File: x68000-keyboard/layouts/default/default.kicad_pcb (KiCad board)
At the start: 4 copper layers, 29.6 x 12.2 mm, 15 parts

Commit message: 両基板: MCU〜レベルシフタ間の信号ネットに用途名を付与
物理ピン名 (PB8, PA3 など) のままでは .ato ソースも生成回路図/ネットリスト
も読みづらいため、MCU 側〜レベルシフタ A 側に中間 signal を挿し、
has_net_name トレイトで用途名 (KEY_TXD_3V3, UP_3V3 など) を割り当てる。
KiCad 上のネット名表示も意味のある名前になる。

Co-Authored-By: Claude Opus 4.7 (1M context) <noreply@anthropic.com>
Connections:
- net PB10 renamed KEY_RXD_3V3
- net PB11 renamed KEY_TXD_3V3
- net PB12_T1C4_T2C2N_ renamed READY_3V3
- net PB8 renamed REMOTE_3V3
- net PB9_T1C1_MCO_TX4_ renamed MSDATA_3V3
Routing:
- net GND: track 4.00 -> 7.88 mm, vias 2 -> 3

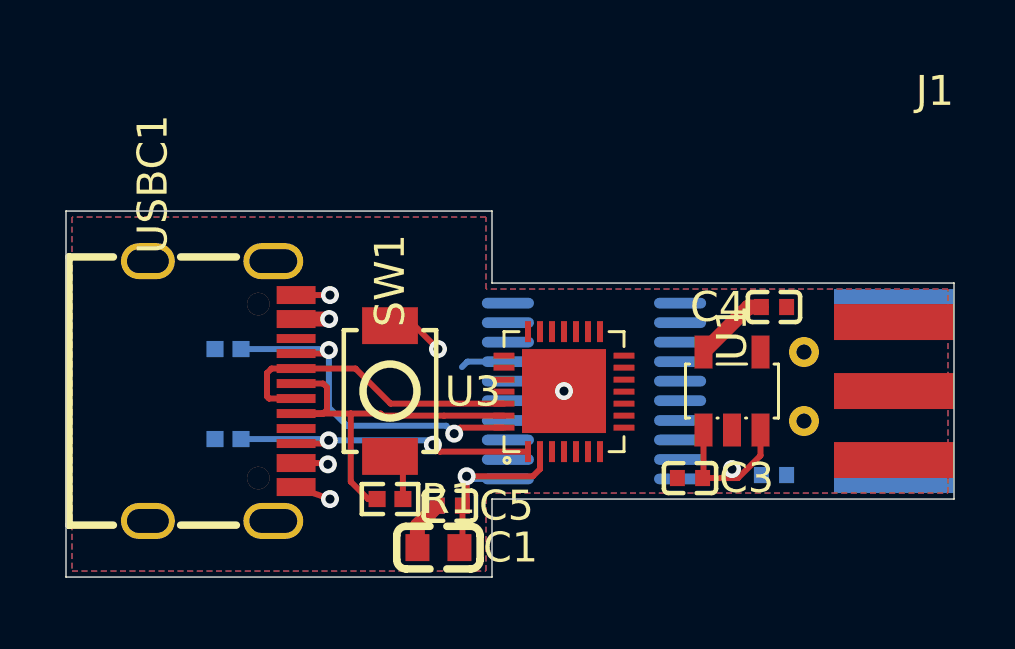
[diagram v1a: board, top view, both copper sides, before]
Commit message: x68000-keyboard: PCB レイアウト初版完了
PCB の配置と配線を一通り完了。レイアウトを進めるうえでフットプリントと
レベルシフタ割当も以下のように調整した。

- レベルシフタのチャネル割当を a1〜a5 から a4〜a8 に変更 (配線取り回しを
  優先)。未使用となった a1〜a3 は GND 落としに切り替え。
- Mini-DIN 7pin: ピン 1/2 のスルーホールパッドを 1.0mm → 0.8mm に縮小、
  ドリルは 0.5mm 維持
- USB-C コネクタフットプリント: pcbnew 上でシルク / 機械パッド表記を整理

DRC 警告は一部残置 (次のパスで詰める)。

Co-Authored-By: Claude Opus 4.7 (1M context) <noreply@anthropic.com>
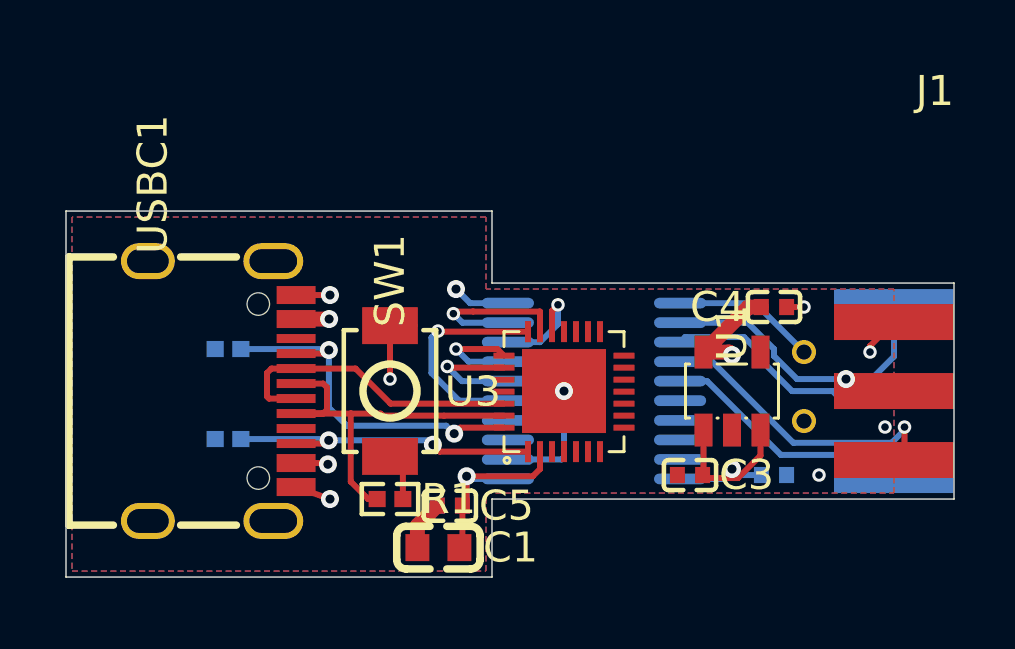
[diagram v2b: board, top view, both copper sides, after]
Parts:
- moved C3 0.10 mm to (171.2, 98.8)
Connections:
- U2 pad 11: b8 -> msdata
- U2 pad 12: b7 -> remote
- U2 pad 13: b6 -> key_txd
- U2 pad 14: remote -> ready
- U2 pad 15: msdata -> key_rxd
- U2 pad 16: ready -> b3
- U2 pad 17: key_rxd -> b2
- U2 pad 18: key_txd -> b1
- U2 pad 2: KEY_TXD_3V3 -> GND
- U2 pad 3: KEY_RXD_3V3 -> GND
- U2 pad 4: READY_3V3 -> GND
- U2 pad 5: MSDATA_3V3 -> KEY_RXD_3V3
- U2 pad 6: REMOTE_3V3 -> READY_3V3
- U2 pad 7: GND -> KEY_TXD_3V3
- U2 pad 8: GND -> REMOTE_3V3
- U2 pad 9: GND -> MSDATA_3V3
- USBC1 pad 1: shell -> GND
- USBC1 pad 2: shell -> GND
- USBC1 pad 3: shell -> GND
- USBC1 pad 4: shell -> GND
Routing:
- net key_txd: track 0.00 -> 10.4 mm
- net ready: track 0.00 -> 10.1 mm, vias 0 -> 1
- net key_rxd: track 0.00 -> 8.43 mm
- net KEY_RXD_3V3: track 0.00 -> 7.43 mm, vias 0 -> 1
- net VDD33: track 12.9 -> 19.4 mm, vias 2 -> 3
- net remote: track 0.00 -> 6.45 mm, vias 0 -> 1
- net GND: track 7.88 -> 14.2 mm, vias 3 -> 8
- net MSDATA_3V3: track 0.00 -> 6.32 mm, vias 0 -> 1
- net msdata: track 0.00 -> 4.81 mm
- net READY_3V3: track 0.00 -> 4.13 mm, vias 0 -> 1
- net KEY_TXD_3V3: track 0.00 -> 3.60 mm, vias 0 -> 1
- net REMOTE_3V3: track 0.00 -> 3.54 mm, vias 0 -> 1
- net VBUS: track 11.3 -> 9.84 mm

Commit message: x68000-keyboard: DRC 警告を解消するためフットプリント / レイアウトを調整
USB-C と TSSOP-20 (TC7MPB9307FT) のシルク線幅を 0.25mm → 0.2mm に縮めて
パッド近接警告を回避。あわせて PCB レイアウトも微修正。

Co-Authored-By: Claude Opus 4.7 (1M context) <noreply@anthropic.com>
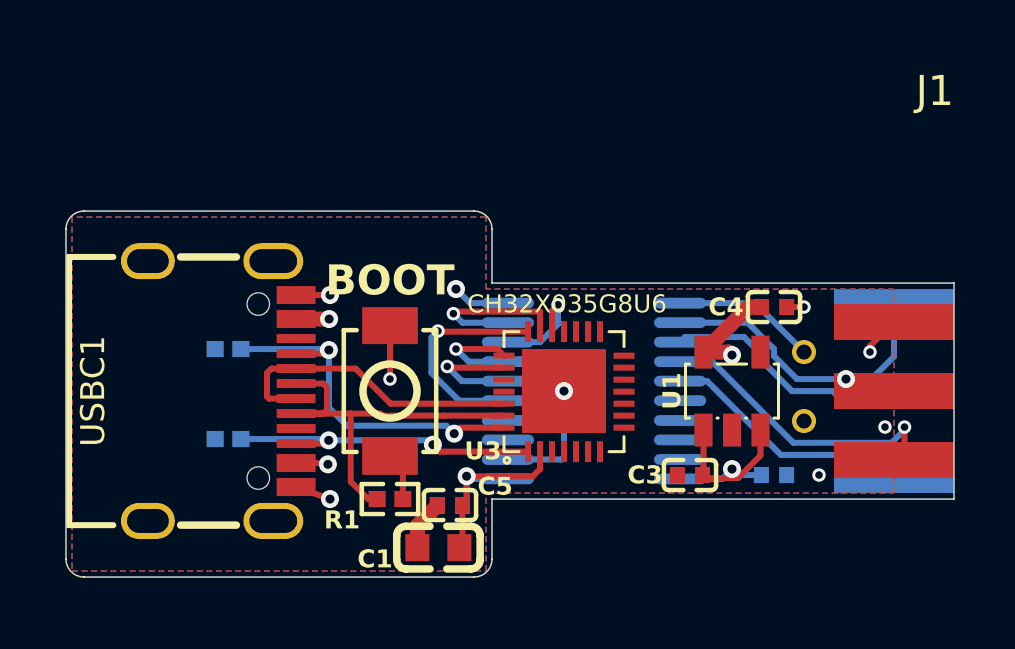
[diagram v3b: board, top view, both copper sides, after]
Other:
- outline, holes or cut-outs redrawn
- board text added: "5.1K"
- board text added: "BOOT"
- board text added: "CH32X035G8U6"
- board text added: "TC7 MPB9307FT"

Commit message: x68000-keyboard: PCB レイアウト調整
Co-Authored-By: Claude Opus 4.7 (1M context) <noreply@anthropic.com>
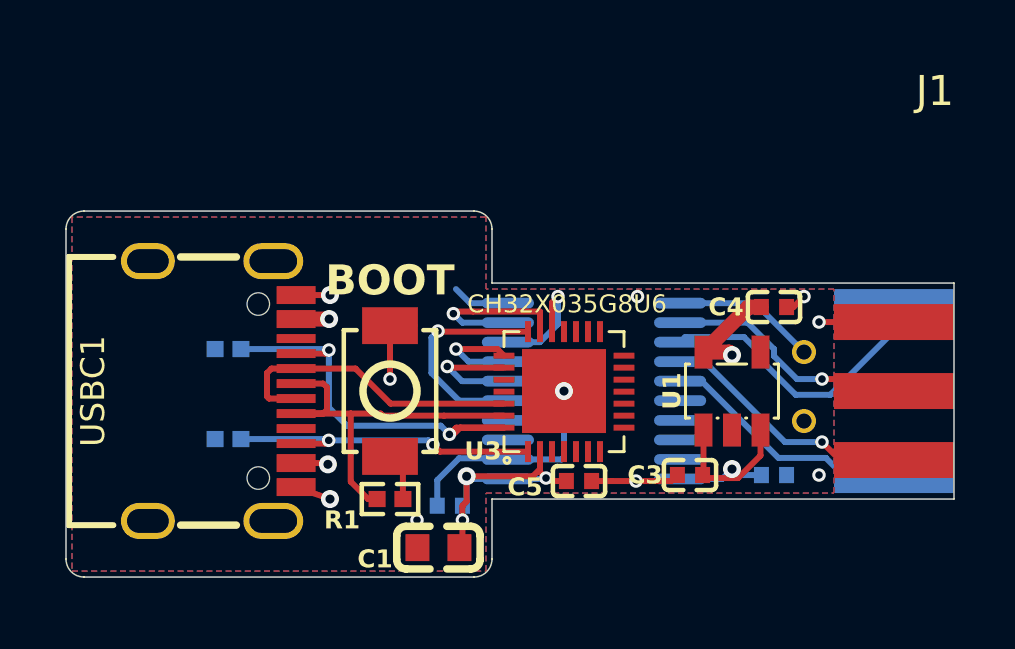
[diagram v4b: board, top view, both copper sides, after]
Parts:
- moved C5 4.37 mm to (167.5, 99.0), turned to 0 degrees
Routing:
- net GND: track 14.2 -> 20.2 mm, vias 8 -> 9
- net VDD33: track 19.4 -> 22.9 mm, vias 3 -> 5
- net remote: track 6.45 -> 8.21 mm
- net PC14_CC1_T1C3_T2C2_: track 12.3 -> 14.0 mm
- net ready: track 10.1 -> 8.98 mm
- net key_txd: track 10.4 -> 9.80 mm
- net REMOTE_3V3: track 3.54 -> 4.09 mm

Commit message: x68000-keyboard: Vcc2 受け入れと最新レイアウトに合わせて .ato / README を整理
直近の設計変更 (Vcc2 をレベルシフタ B 側電源に採用、レベルシフタチャネル
割当を a1〜a5 → a4〜a8 に再配置、Mini-DIN フットプリント自作完了) に対し
.ato のコメントと README の記述が追従していなかったので整合させる。

- .ato: docstring に 3 電源レール構成を追記、接続マップコメントを実装通り
  a6/a4/a5/a8/a7 に修正、未使用 GND 落とし範囲も a1/a2/a3 に訂正
- README: ピン割当表のレベルシフタ列を a4〜a8 系に書き換え、Mini-DIN を
  「プレースホルダ」表記から「自作実装済み」に更新、電源セクションを
  VBUS / VDD33 / VCC2 の 3 レール構成として全面書き直し

Co-Authored-By: Claude Opus 4.7 (1M context) <noreply@anthropic.com>
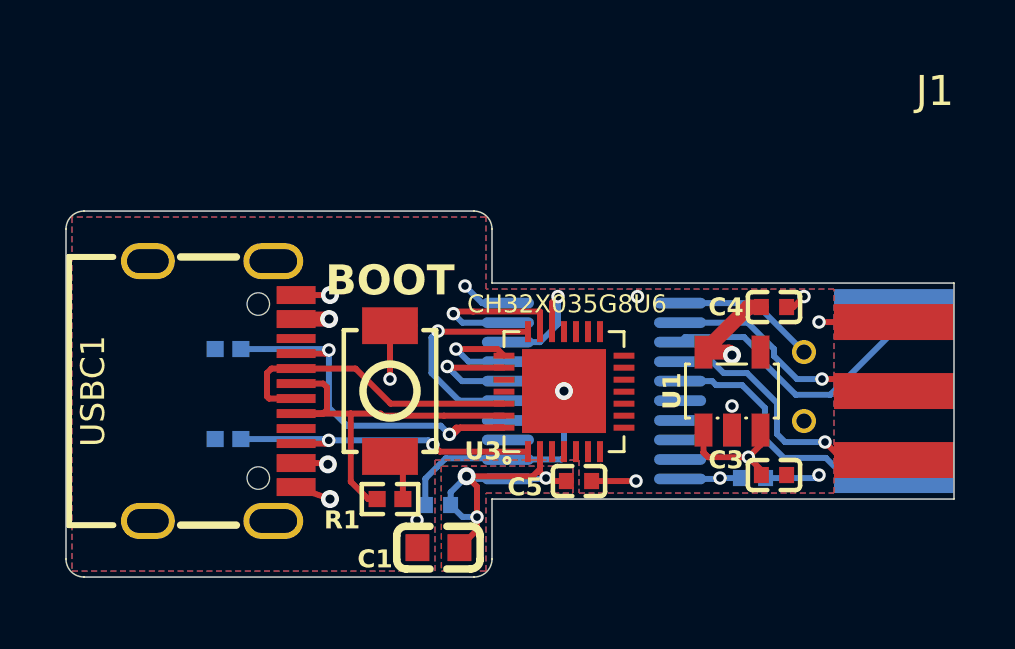
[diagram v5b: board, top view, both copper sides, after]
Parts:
- moved C3 2.80 mm to (174.0, 98.8), turned to 0 degrees
- moved C6 0.71 mm to (173.3, 98.9)
- moved C2 0.40 mm to (162.8, 99.8)
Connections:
- C6 pad 1: VBUS -> VCC2
- J1 pad 1: vcc2 -> VCC2
- U2 pad 20: VBUS -> VCC2
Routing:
- net VCC2: track 0.00 -> 6.49 mm, vias 0 -> 1
- net VBUS: track 9.84 -> 6.55 mm
- net ready: track 8.98 -> 11.6 mm
- net GND: track 20.2 -> 21.5 mm, vias 9 -> 11
- net VDD33: track 22.9 -> 23.7 mm
- net key_rxd: track 8.43 -> 9.03 mm
- added copper zone on B.Cu, net VDD33
- added copper zone on F.Cu, net VDD33

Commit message: x68000-keyboard: 電源 LED とフルカラー LED (WS2812B-2020) を追加
atari-joystick と同じ流儀で 2 種類の LED を実装:

- LED1 (緑 0603, Hubei KT-0603G, C12624) + R4 (1kΩ): VDD33 常時点灯の
  電源インジケータ
- LED2 (Worldsemi WS2812B-2020, C965555): シリアル制御 RGB LED。
  MCU PB0 (QFN28 Pin 13) → R5 (470Ω 直列ダンピング) → DI で駆動。
  VDD33 共通電源
- parts/leds.ato を atari-joystick と同期 (LedGreenKT0603 / LedRgbWs2812b)
- README のピン割当表と LED 記述を更新

Co-Authored-By: Claude Opus 4.7 (1M context) <noreply@anthropic.com>
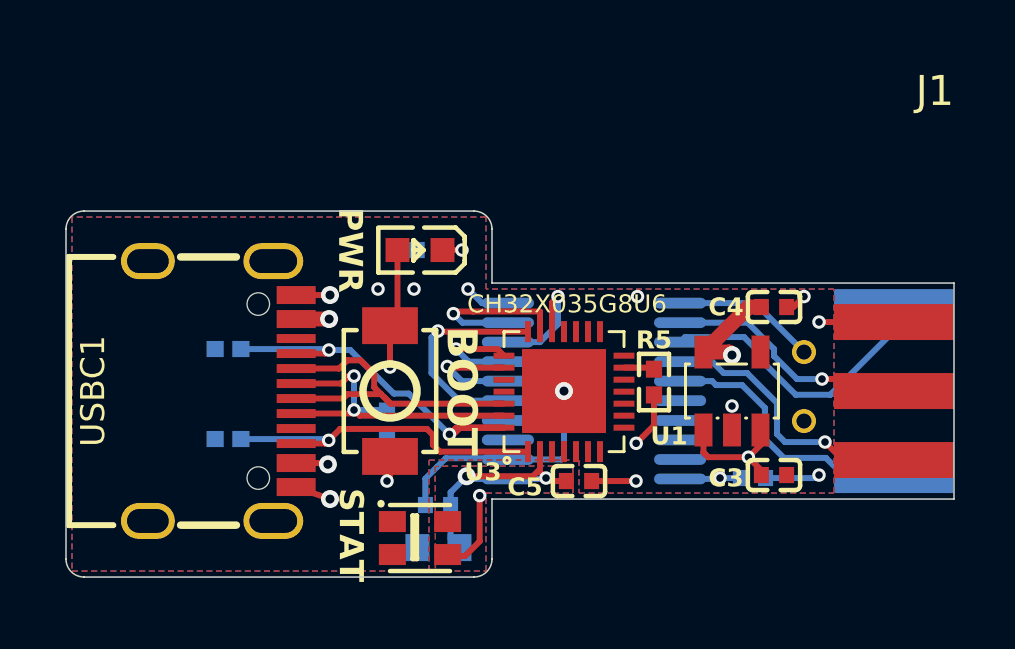
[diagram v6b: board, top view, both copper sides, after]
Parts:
- added LED1: , Hubei_KENTO_Elec_KT_0603G:LED0603-RD, F.Cu at (162.2, 91.3)
- added LED2: , Worldsemi_WS2812B_2020:LED-SMD_4P-L2.0-W2.0-TL_WS2812B-2020, F.Cu at (162.2, 100.9)
- added R4: 1kΩ ±1%, UNI_ROYAL_0402WGF1001TCE:R0402, B.Cu at (162.5, 91.3)
- added R5: 470Ω ±1%, UNI_ROYAL_0402WGF4700TCE:R0402, F.Cu at (170.0, 95.7)
- C1, R1: moved to B.Cu
- moved R1 2.50 mm to (161.1, 97.1), turned to 90 degrees
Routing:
- net din: track 0.00 -> 10.7 mm, vias 0 -> 2
- net dp: track 13.3 -> 11.2 mm, vias 0 -> 2
- net terminal_b: track 1.60 -> 2.94 mm, vias 0 -> 1
- net cathode: track 0.00 -> 1.32 mm, vias 0 -> 1
- net PC14_CC1_T1C3_T2C2_: track 14.0 -> 12.9 mm
- net PB0: track 0.00 -> 1.02 mm
- net GND: track 21.5 -> 20.6 mm, vias 11 -> 12
- net dn: track 10.2 -> 11.1 mm
- net PC15_CC2_T2C3_T1ET_: track 10.9 -> 11.4 mm, vias 2 -> 1
- net VDD33: track 23.7 -> 24.0 mm, vias 5 -> 4
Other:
- board text added: "PWR"
- board text added: "STAT"

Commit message: 両基板 v1.0.0: JLCPCB 発注用ファイル一式を確定
atari-joystick / x68000-keyboard ともに JLCPCB PCBA 発注用の Gerber ZIP /
BOM / CPL (positions) / designators を `layouts/default/production/` 配下に
v1.0.0 名義で固定。fabrication-toolkit プラグインの設定も合わせて記録する。

実発注に送付したファイル:
- atari-joystick/layouts/default/production/MimicX-Joystick-v1.0.0.zip 他
- x68000-keyboard/layouts/default/production/MimicX-Keyboard-v1.0.0.zip 他

Co-Authored-By: Claude Opus 4.7 (1M context) <noreply@anthropic.com>
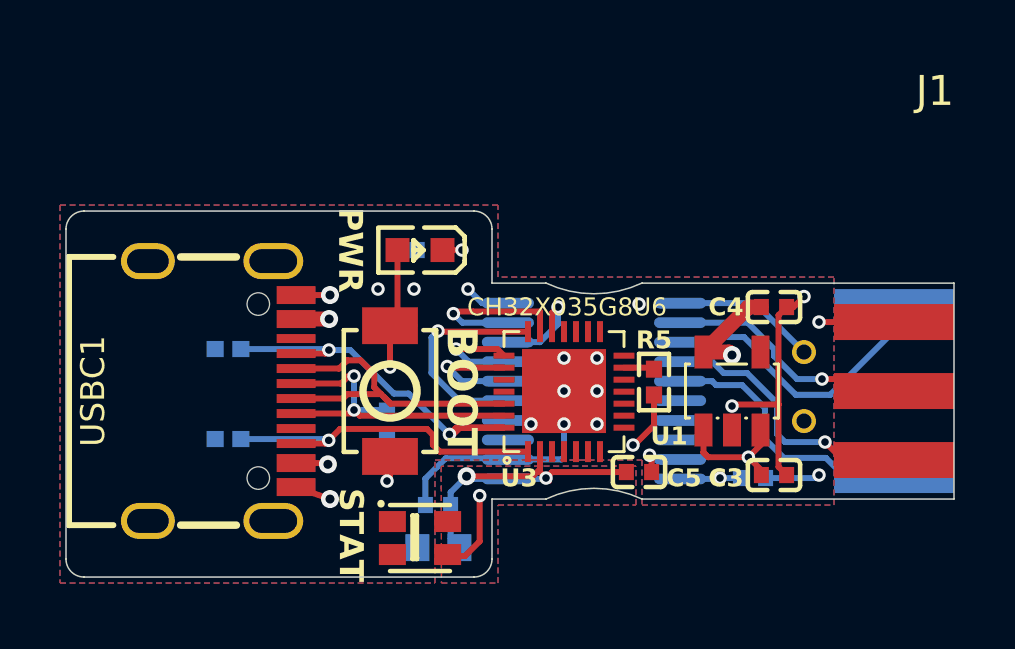
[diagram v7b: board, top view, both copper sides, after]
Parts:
- moved C5 2.02 mm to (169.5, 98.7)
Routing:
- net GND: track 20.6 -> 25.6 mm, vias 12 -> 18
- net VDD33: track 24.0 -> 26.2 mm
- net din: track 10.7 -> 11.6 mm
- net REMOTE_3V3: track 4.09 -> 3.39 mm
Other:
- outline, holes or cut-outs redrawn
- board text added: "Mimic X Adapter"
- board text added: "X68000 KBD"
- board text added: "v1.0.0 @kunichiko"

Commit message: x68000-keyboard v1.0.1: 基板外形のセンターずれ修正と Mini-DIN ピン穴の拡大
- 基板外形を Y 方向に 0.1mm 移動 (90.0-102.2 → 89.9-102.1)。コネクタ中心
  (Y=96.0) から上下の基板端までが 2.5mm / 2.5mm になるはずが、片側に 0.1mm
  ずれていた。LED などエッジ基準の部品も追従
- MiniDIN_7P_X68000: ピン 1 / 2 のスルーホールを φ0.5 → φ0.8 (パッド 0.8 →
  1.2mm) に拡大し、位置を外側へ 0.12mm 移動 (Y 1.0 → 1.12 / -1.3 → -1.42)
- C3 / C4 / C6 / U1 の配置調整と再配線
- 製造データを MimicX-Keyboard-v1.0.1 で出し直し (BOM 変更なし)

Co-Authored-By: Claude Opus 5.5 <noreply@anthropic.com>
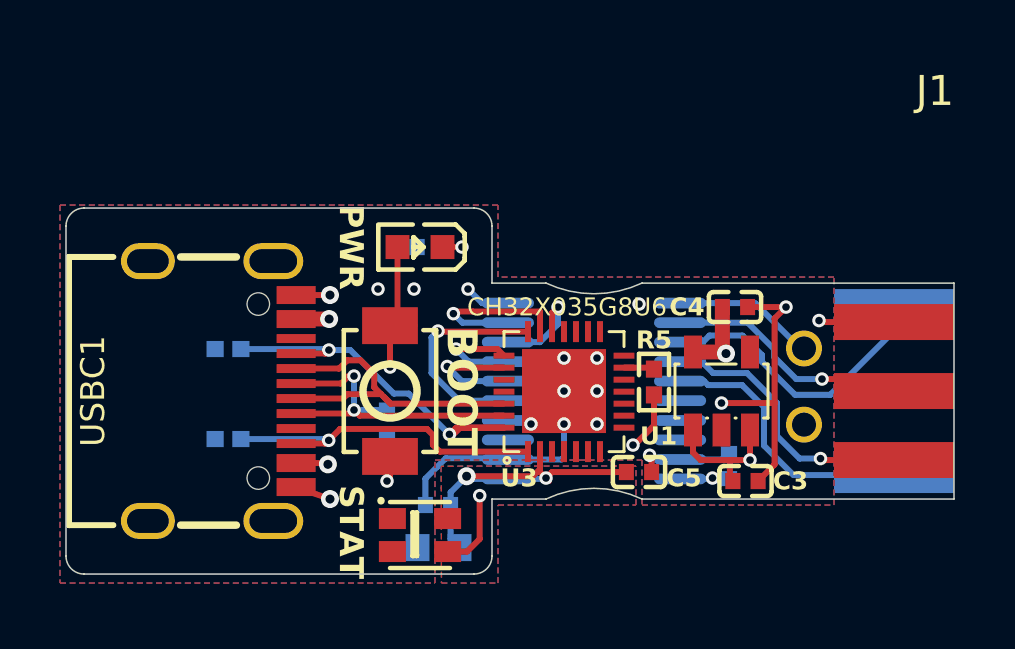
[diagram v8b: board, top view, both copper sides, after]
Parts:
- moved C4 1.30 mm to (172.7, 93.2)
- moved C3 0.97 mm to (173.1, 99.0)
- moved C6 0.89 mm to (172.5, 98.5), turned to 90 degrees
- moved U1 0.35 mm to (172.2, 96.0)
- moved LED2 0.10 mm to (162.2, 100.8)
- moved LED1 0.10 mm to (162.2, 91.2)
- moved R4 0.10 mm to (162.5, 91.2)
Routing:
- net key_rxd: track 9.03 -> 11.0 mm
- net ready: track 11.6 -> 9.65 mm
- net GND: track 25.6 -> 26.8 mm, vias 18 -> 17
- net VDD33: track 26.2 -> 25.4 mm
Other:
- outline, holes or cut-outs redrawn
- board text added: "v1.0.1 @kunichiko"
- board text removed: "v1.0.0 @kunichiko"
